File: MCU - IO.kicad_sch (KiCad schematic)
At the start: 1 part, among them U1 STM32H743ZIT6TR

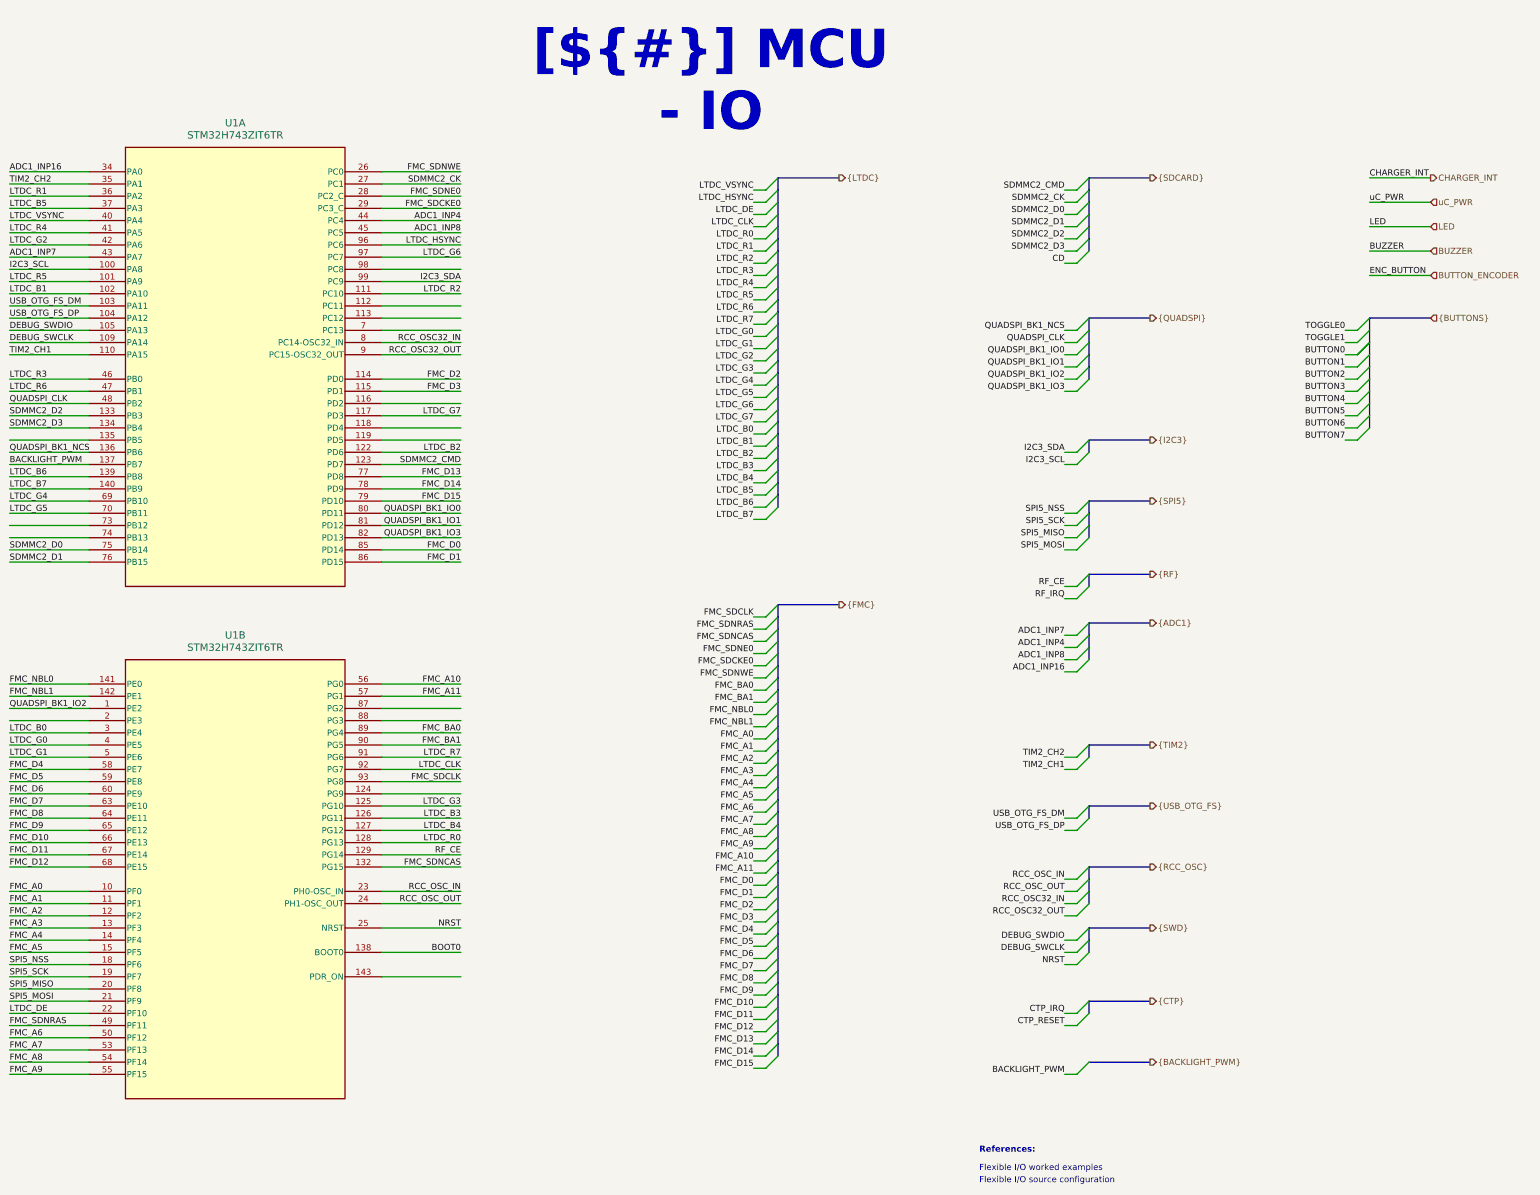
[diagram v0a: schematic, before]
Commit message: added gpio expander, uc pinout, unused gpio connector, i2c pullup, delete unused files
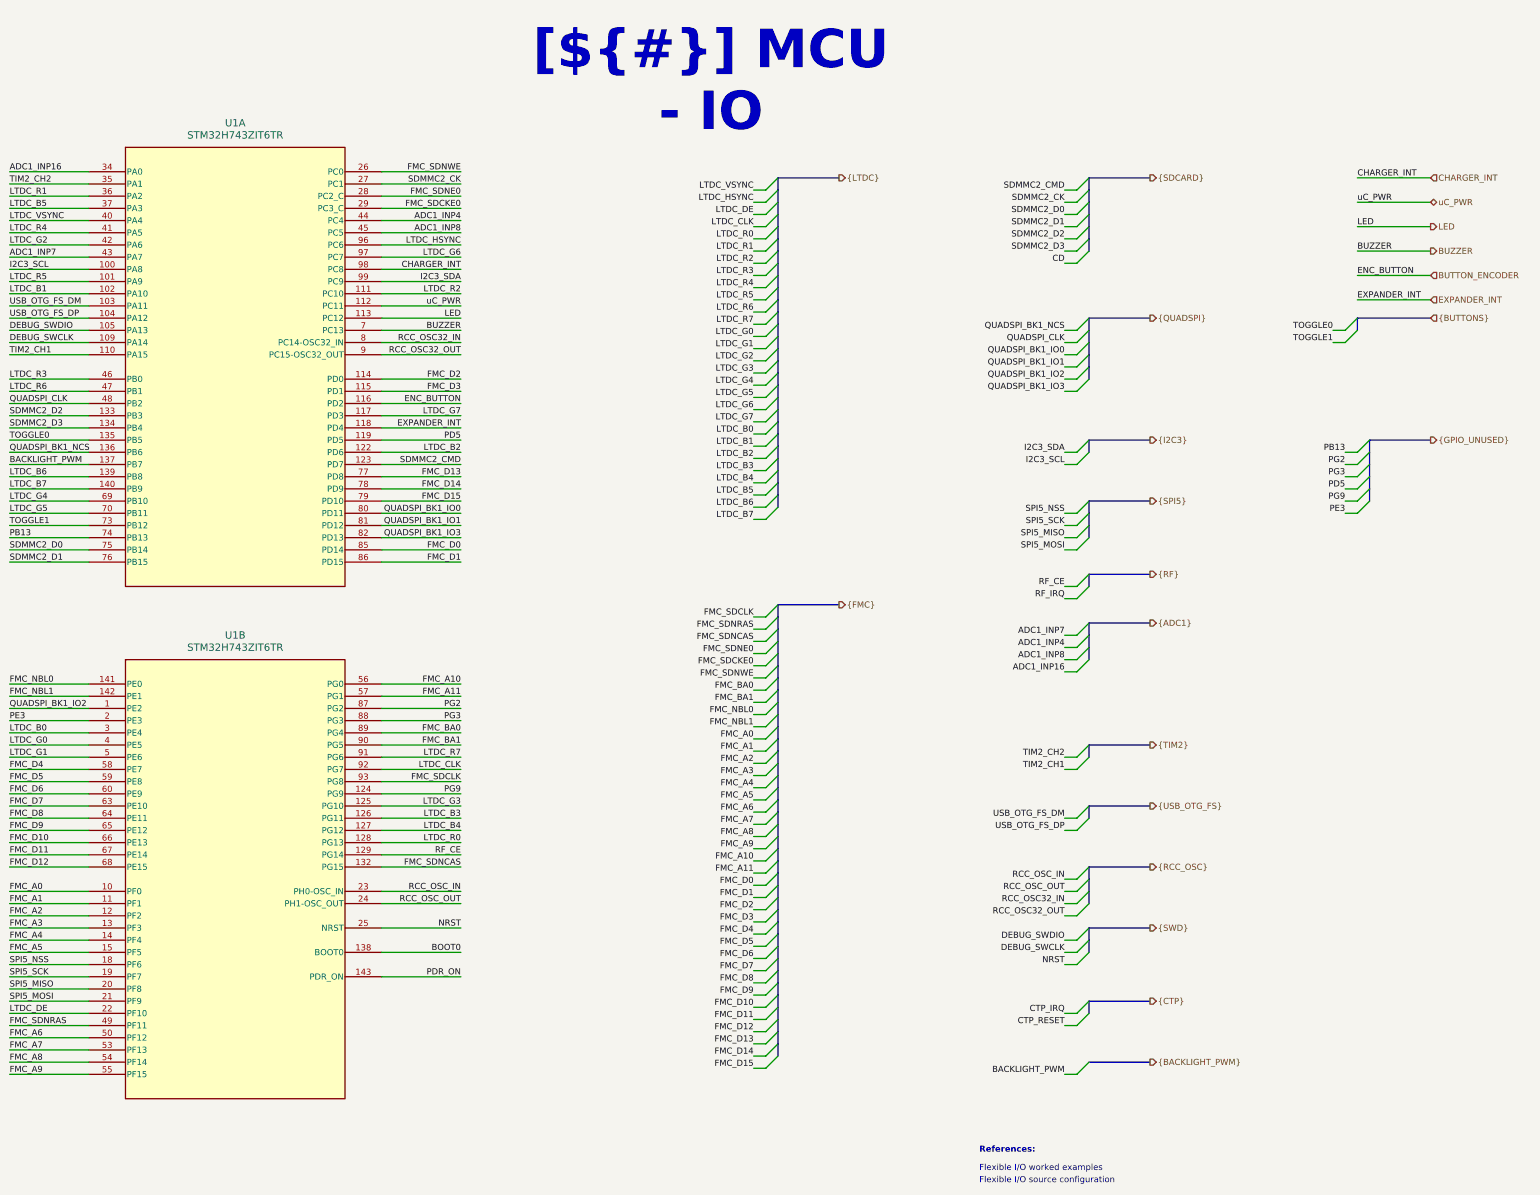
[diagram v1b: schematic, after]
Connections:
- net BUTTON_ENCODER: now also U1.116 (PD2)
- net BUZZER: now also U1.7 (PC13)
- net CHARGER_INT: now also U1.98 (PC8)
- net LED: now also U1.113 (PC12)
- net TOGGLE0: now also U1.135 (PB5)
- net TOGGLE1: now also U1.73 (PB12)
- net uC_PWR: now also U1.112 (PC11)
- net EXPANDER_INT: now reaches U1.118 (PD4)
- net PD5: now reaches U1.119 (PD5)
- net PB13: now reaches U1.74 (PB13)
- net PG9: now reaches U1.124 (PG9)
- net PDR_ON: now reaches U1.143 (PDR_ON)
- net PE3: now reaches U1.2 (PE3)
- net PG2: now reaches U1.87 (PG2)
- net PG3: now reaches U1.88 (PG3)

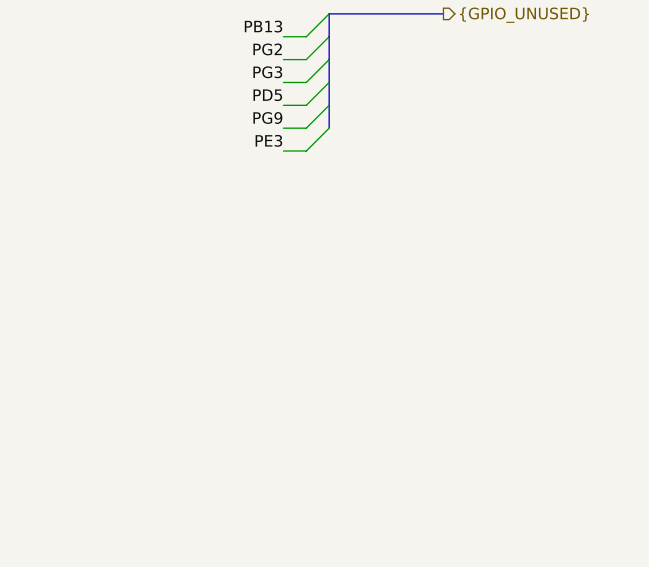
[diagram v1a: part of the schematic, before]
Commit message: added 2pin 2.54 male header and connect boot0, pdr_on signals
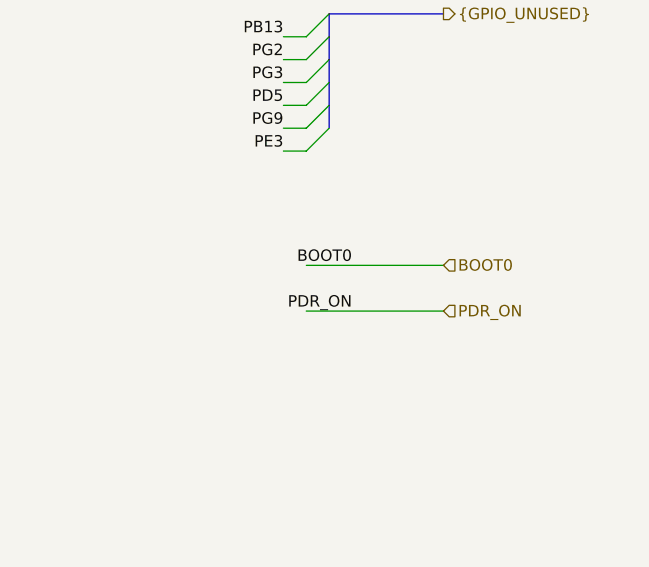
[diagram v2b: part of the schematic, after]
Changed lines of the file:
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@@
 		)
 	)
+	(wire
+		(pts
+			(xy 359.41 129.54) (xy 344.17 129.54)
+		)
+		(stroke
+			(width 0)
+			(type default)
+		)
+	)
 	(bus
 		(pts
@@
 	(wire
 		(pts
+			(xy 344.17 134.62) (xy 359.41 134.62)
+		)
+		(stroke
+			(width 0)
+			(type default)
+		)
+	)
+	(wire
+		(pts
 			(xy 80.01 152.4) (xy 63.5 152.4)
 		)
@@
 		)
 	)
+	(label "PDR_ON"
+		(at 349.25 134.62 180)
+		(effects
+			(font
+				(size 1.27 1.27)
+			)
+			(justify right bottom)
+		)
+	)
 	(label "LTDC_B3"
 		(at 218.44 107.95 180)
@@
 		)
 	)
+	(label "BOOT0"
+		(at 349.25 129.54 180)
+		(effects
+			(font
+				(size 1.27 1.27)
+			)
+			(justify right bottom)
+		)
+	)
 	(label "USB_OTG_FS_DP"
 		(at 283.21 182.88 180)
@@
 		)
 	)
+	(hierarchical_label "PDR_ON"
+		(shape input)
+		(at 359.41 134.62 0)
+		(effects
+			(font
+				(size 1.27 1.27)
+			)
+			(justify left)
+		)
+	)
 	(hierarchical_label "{GPIO_UNUSED}"
 		(shape output)
@@
 		(effects
 			(font
+				(size 1.27 1.27)
+			)
+			(justify left)
+		)
+	)
+	(hierarchical_label "BOOT0"
+		(shape input)
+		(at 359.41 129.54 0)
+		(effects
+			(font

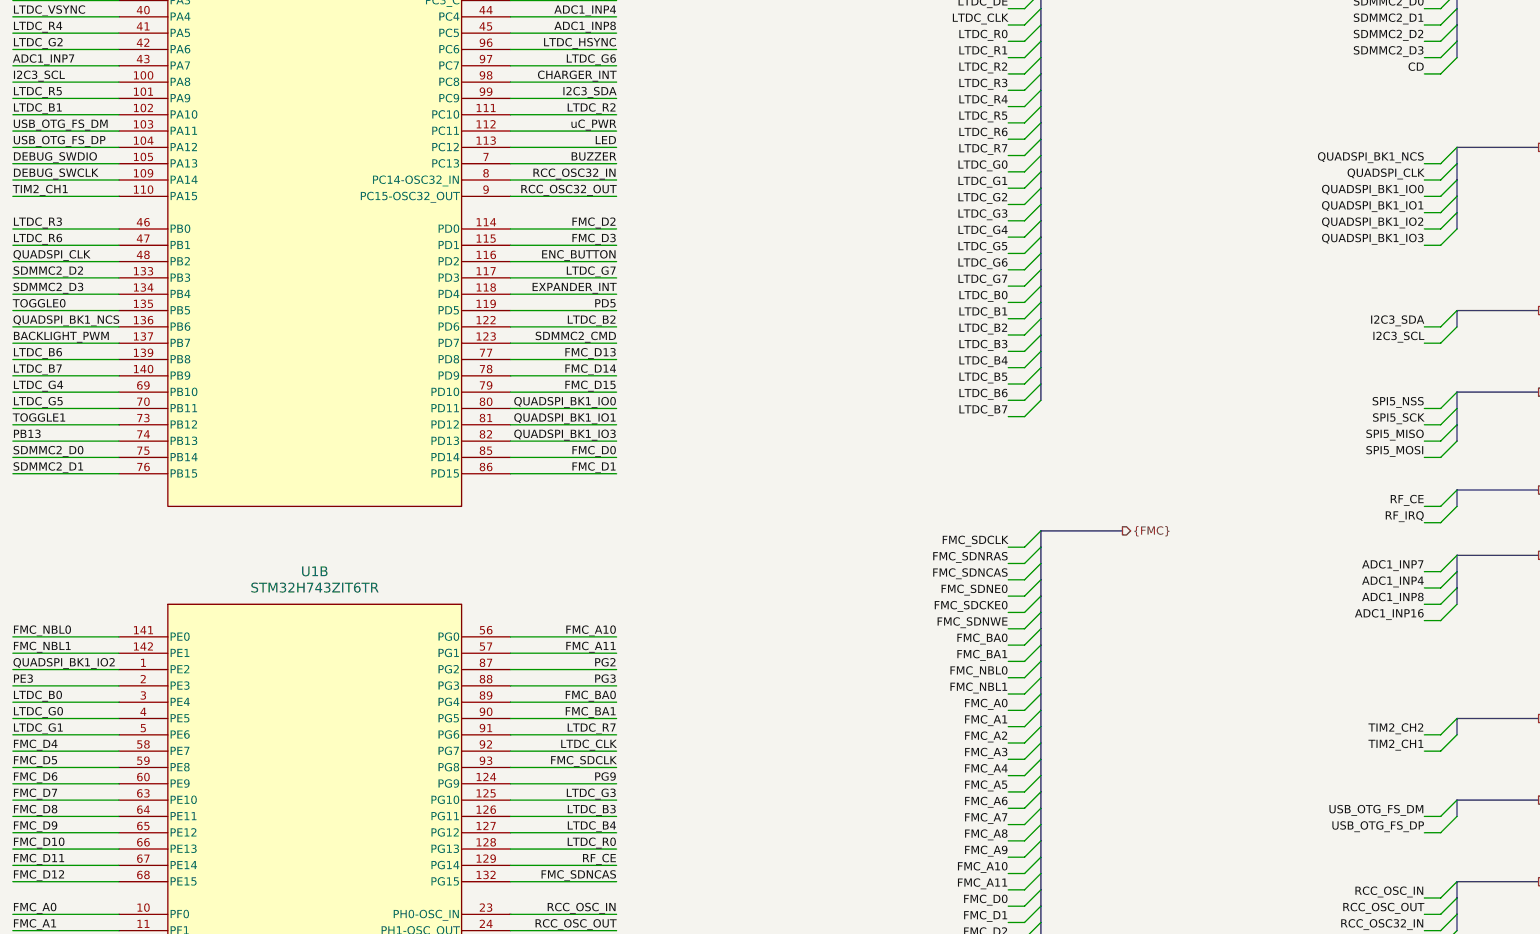
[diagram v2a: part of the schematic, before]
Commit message: duzo zmian, layout przetwornic i zasilania, wstepny routing sd card impedance control, usb differential impedance control
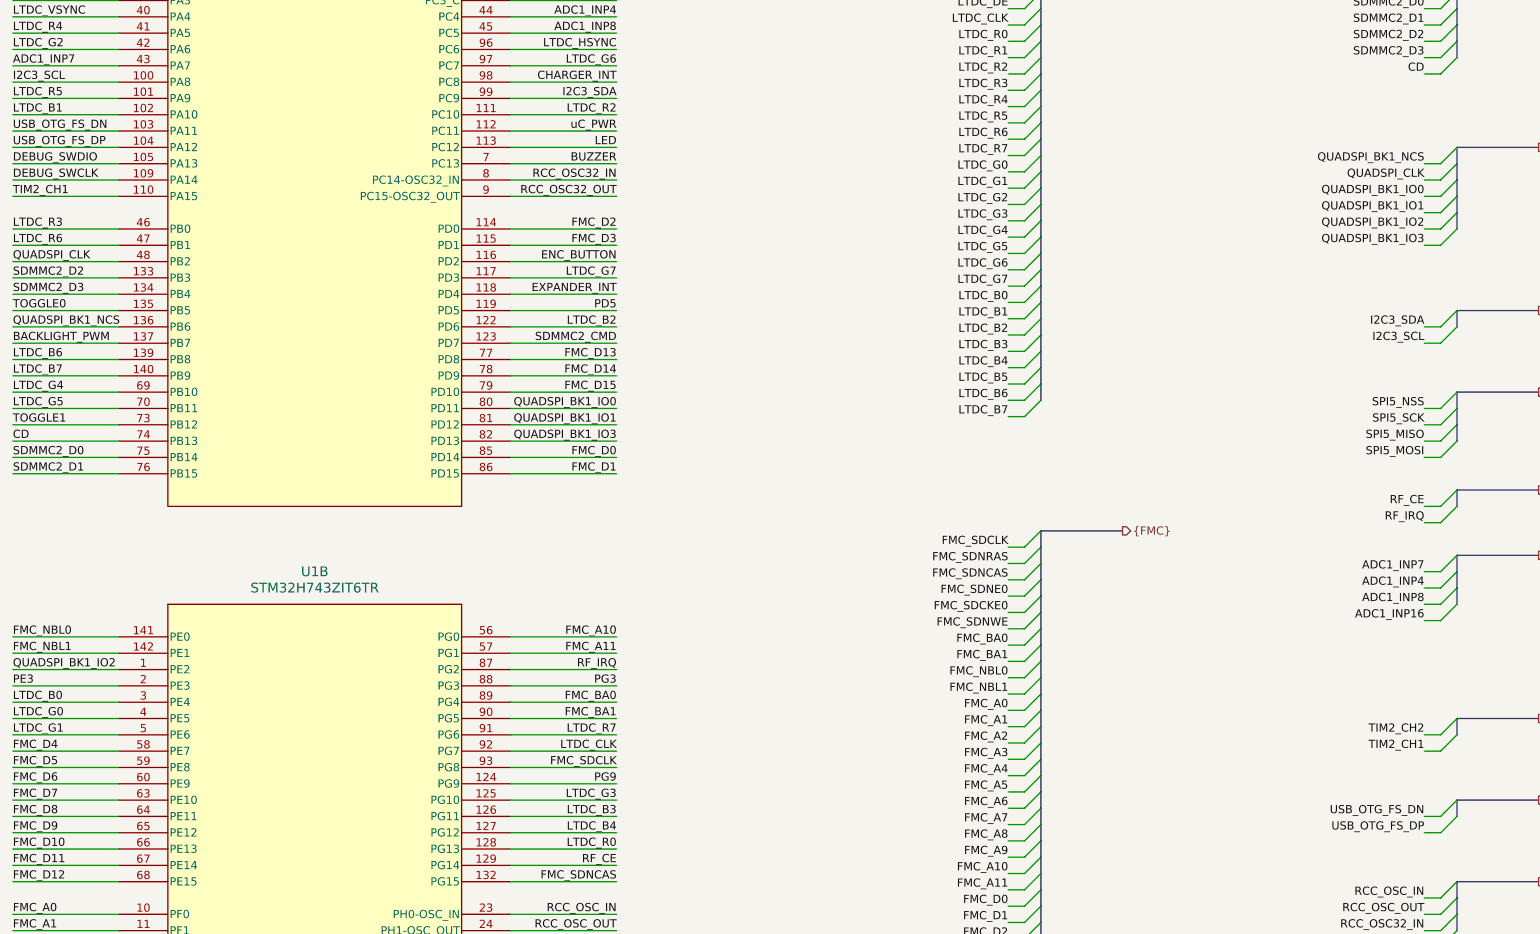
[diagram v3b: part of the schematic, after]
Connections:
- net CD: now also U1.74 (PB13)
- net PB13: no longer U1.74 (PB13)
- net PG2: no longer U1.87 (PG2)
- net RF_IRQ: now also U1.87 (PG2)
- net USB_OTG_FS_DM renamed USB_OTG_FS_DN
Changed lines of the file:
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@@
 		(members "TIM2_CH2" "TIM2_CH1")
 	)
-	(bus_alias "USB_OTG_FS"
-		(members "USB_OTG_FS_DM" "USB_OTG_FS_DP")
-	)
 	(text "Flexible I/O worked examples"
 		(exclude_from_sim no)
@@
 		)
 	)
-	(label "USB_OTG_FS_DM"
+	(label "USB_OTG_FS_DN"
 		(at 63.5 73.66 0)
 		(effects
@@
 		)
 	)
-	(label "PG2"
-		(at 157.48 157.48 180)
-		(effects
-			(font
-				(size 1.27 1.27)
-			)
-			(justify right bottom)
-		)
-	)
 	(label "FMC_D5"
 		(at 63.5 172.72 0)
@@
 		)
 	)
+	(label "CD"
+		(at 63.5 121.92 0)
+		(effects
+			(font
+				(size 1.27 1.27)
+			)
+			(justify left bottom)
+		)
+	)
 	(label "DEBUG_SWDIO"
 		(at 63.5 78.74 0)
@@
 		)
 	)
-	(label "PB13"
-		(at 63.5 121.92 0)
-		(effects
-			(font
-				(size 1.27 1.27)
-			)
-			(justify left bottom)
-		)
-	)
 	(label "SDMMC2_D1"
 		(at 283.21 57.15 180)
@@
 		)
 	)
-	(label "USB_OTG_FS_DM"
+	(label "USB_OTG_FS_DN"
 		(at 283.21 180.34 180)
 		(effects
@@
 		(effects
 			(font
+				(size 1.27 1.27)
+			)
+			(justify right bottom)
+		)
+	)
+	(label "RF_IRQ"
+		(at 157.48 157.48 180)
+		(effects
+			(font
